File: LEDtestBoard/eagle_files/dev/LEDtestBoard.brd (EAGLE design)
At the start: 30 x 50 mm, 18 parts, among them SW1 PCM12SMTR, SW2 PCM12SMTR, SW3 PCM12SMTR, SW4 PCM12SMTR, SW5 PCM12SMTR, SW6 PCM12SMTR, SW7 PCM12SMTR, SW8 PCM12SMTR

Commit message: Updated LEDtestBoard dev files. Ready to begin pad check and routing.
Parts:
- added D1, D2: SZA05A0A, freddyLibr:SZA05A0A
- added D3: XLAMP_COLOR, freddyLibr:8-SMD-LED
- added D4, D5: LACN5MFBGB241Z, freddyLibr:2-SMD-LED-NO-EXP
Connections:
- net N$6 renamed GND
- new net N$13: D3.1, SW5.2
- new net N$14: D3.2, SW6.2
- new net N$15: D3.3, SW7.2
- new net N$16: D3.4, SW8.2
- new net N$17: D3.8, R5.2
- new net N$18: D3.7, R6.2
- new net N$19: D3.6, R7.2
- new net N$20: D3.5, R8.2
- net N$10: now also D5.2, R4.2; no longer R8.2, SW8.2
- net N$2: now also D1.12, D1.2; no longer SW1.2
- net N$3: now also D1.1, D1.11, SW1.2; no longer R2.2, SW2.2
- net N$4: now also D2.1, D2.11, SW2.2; no longer R3.2, SW3.2
- net N$5: now also D2.12, D2.2, R2.2; no longer R4.2, SW4.2
- net N$7: now also D4.2, R3.2; no longer R5.2, SW5.2
- net N$8: now also D4.1, SW3.2; no longer R6.2, SW6.2
- net N$9: now also D5.1, SW4.2; no longer R7.2, SW7.2
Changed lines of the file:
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@@
 <element name="R7" library="resistor" package="R0603" value="" x="18.86" y="40.48" rot="MR0"/>
 <element name="R8" library="resistor" package="R0603" value="" x="21.23" y="23.14" rot="MR180"/>
+<element name="D3" library="freddyLibr" package="8-SMD-LED" value="XLAMP_COLOR" x="14.64" y="27.42" rot="MR0"/>
+<element name="D4" library="freddyLibr" package="2-SMD-LED-NO-EXP" value="LACN5MFBGB241Z" x="20.6" y="28.05" rot="R270"/>
+<element name="D5" library="freddyLibr" package="2-SMD-LED-NO-EXP" value="LACN5MFBGB241Z" x="19.66" y="21.11" rot="R270"/>
+<element name="D1" library="freddyLibr" package="SZA05A0A" value="SZA05A0A" x="10.5" y="21.13"/>
+<element name="D2" library="freddyLibr" package="SZA05A0A" value="SZA05A0A" x="9.44" y="28.84"/>
 </elements>
 <signals>
@@
 <wire x1="4.18" y1="35.74" x2="4.08" y2="17.38" width="0" layer="19" extent="1-1"/>
 </signal>
-<signal name="N$6">
+<signal name="GND">
 <contactref element="JP1" pad="1"/>
 <contactref element="R1" pad="1"/>
@@
 <contactref element="SW7" pad="3"/>
 <contactref element="SW8" pad="3"/>
-<wire x1="20.12" y1="33.38" x2="25.62" y2="35.62" width="0" layer="19" extent="1-1"/>
-<wire x1="8.2" y1="33.49" x2="20.12" y2="33.38" width="0" layer="19" extent="1-1"/>
-<wire x1="4.18" y1="31.24" x2="8.2" y2="33.49" width="0" layer="19" extent="1-1"/>
-<wire x1="25.5" y1="17.4" x2="20.12" y2="33.38" width="0" layer="19" extent="1-1"/>
+<wire x1="19.71" y1="40.48" x2="24.9" y2="45.85" width="0" layer="19" extent="16-16"/>
+<wire x1="20.12" y1="33.38" x2="19.71" y2="40.48" width="0" layer="19" extent="1-16"/>
+<wire x1="25.62" y1="35.62" x2="20.12" y2="33.38" width="0" layer="19" extent="1-1"/>
+<wire x1="20.38" y1="23.14" x2="20.12" y2="33.38" width="0" layer="19" extent="1-16"/>
+<wire x1="25.63" y1="21.98" x2="20.38" y2="23.14" width="0" layer="19" extent="16-16"/>
+<wire x1="25.5" y1="17.4" x2="25.63" y2="21.98" width="0" layer="19" extent="1-16"/>
 <wire x1="18.54" y1="14.51" x2="25.5" y2="17.4" width="0" layer="19" extent="1-1"/>
 <wire x1="8.72" y1="14.56" x2="18.54" y2="14.51" width="0" layer="19" extent="1-1"/>
 <wire x1="4.08" y1="12.88" x2="8.72" y2="14.56" width="0" layer="19" extent="1-1"/>
 <wire x1="10.5" y1="8" x2="8.72" y2="14.56" width="0" layer="19" extent="1-1"/>
-<wire x1="4.11" y1="26.89" x2="4.08" y2="12.88" width="0" layer="19" extent="1-1"/>
-<wire x1="9.58" y1="45.94" x2="4.11" y2="26.89" width="0" layer="19" extent="1-1"/>
-<wire x1="24.9" y1="45.85" x2="9.58" y2="45.94" width="0" layer="19" extent="1-1"/>
-<wire x1="25.63" y1="21.98" x2="24.9" y2="45.85" width="0" layer="19" extent="1-1"/>
-<wire x1="7.95" y1="23.07" x2="25.63" y2="21.98" width="0" layer="19" extent="1-1"/>
-<wire x1="8.4" y1="40.21" x2="7.95" y2="23.07" width="0" layer="19" extent="1-1"/>
-<wire x1="19.71" y1="40.48" x2="8.4" y2="40.21" width="0" layer="19" extent="1-1"/>
-<wire x1="20.38" y1="23.14" x2="19.71" y2="40.48" width="0" layer="19" extent="1-1"/>
+<wire x1="7.95" y1="23.07" x2="8.72" y2="14.56" width="0" layer="19" extent="1-16"/>
+<wire x1="4.11" y1="26.89" x2="7.95" y2="23.07" width="0" layer="19" extent="16-16"/>
+<wire x1="4.18" y1="31.24" x2="4.11" y2="26.89" width="0" layer="19" extent="1-16"/>
+<wire x1="8.2" y1="33.49" x2="4.18" y2="31.24" width="0" layer="19" extent="1-1"/>
+<wire x1="8.4" y1="40.21" x2="8.2" y2="33.49" width="0" layer="19" extent="1-16"/>
+<wire x1="9.58" y1="45.94" x2="8.4" y2="40.21" width="0" layer="19" extent="16-16"/>
+</signal>
+<signal name="N$13">
+<contactref element="SW5" pad="2"/>
+<contactref element="D3" pad="1"/>
+<wire x1="12.49" y1="29.36" x2="4.11" y2="25.39" width="0" layer="19" extent="1-16"/>
+</signal>
+<signal name="N$14">
+<contactref element="SW6" pad="2"/>
+<contactref element="D3" pad="2"/>
+<wire x1="12.49" y1="28.05" x2="8.08" y2="45.94" width="0" layer="19" extent="1-16"/>
+</signal>
+<signal name="N$15">
+<contactref element="SW7" pad="2"/>
+<contactref element="D3" pad="3"/>
+<wire x1="12.49" y1="26.79" x2="23.4" y2="45.85" width="0" layer="19" extent="1-16"/>
+</signal>
+<signal name="N$16">
+<contactref element="SW8" pad="2"/>
+<contactref element="D3" pad="4"/>
+<wire x1="12.49" y1="25.48" x2="25.63" y2="23.48" width="0" layer="19" extent="1-16"/>
+</signal>
+<signal name="N$17">
+<contactref element="D3" pad="8"/>
+<contactref element="R5" pad="2"/>
+<wire x1="16.79" y1="29.36" x2="7.95" y2="24.77" width="0" layer="19" extent="1-16"/>
+</signal>
+<signal name="N$18">
+<contactref element="D3" pad="7"/>
+<contactref element="R6" pad="2"/>
+<wire x1="16.79" y1="28.05" x2="6.7" y2="40.21" width="0" layer="19" extent="1-16"/>
+</signal>
+<signal name="N$19">
+<contactref element="D3" pad="6"/>
+<contactref element="R7" pad="2"/>
+<wire x1="16.79" y1="26.79" x2="18.01" y2="40.48" width="0" layer="19" extent="1-16"/>
+</signal>
+<signal name="N$20">
+<contactref element="D3" pad="5"/>
+<contactref element="R8" pad="2"/>
+<wire x1="16.79" y1="25.48" x2="22.08" y2="23.14" width="0" layer="19" extent="1-16"/>
 </signal>
 <signal name="N$2">
 <contactref element="R1" pad="2"/>
-<contactref element="SW1" pad="2"/>
-<wire x1="4.08" y1="14.38" x2="10.42" y2="14.56" width="0" layer="19" extent="1-1"/>
+<contactref element="D1" pad="2"/>
+<contactref element="D1" pad="12"/>
+<wire x1="12.35" y1="21.13" x2="10.42" y2="14.56" width="0" layer="19" extent="1-1"/>
+<wire x1="11.9" y1="21.13" x2="12.35" y2="21.13" width="0" layer="19" extent="1-1"/>
 </signal>
 <signal name="N$3">
-<contactref element="R2" pad="2"/>
-<contactref element="SW2" pad="2"/>
-<wire x1="4.18" y1="32.74" x2="9.9" y2="33.49" width="0" layer="19" extent="1-1"/>
+<contactref element="D1" pad="11"/>
+<contactref element="D1" pad="1"/>
+<contactref element="SW1" pad="2"/>
+<wire x1="9.1" y1="21.13" x2="8.65" y2="21.13" width="0" layer="19" extent="1-1"/>
+<wire x1="4.08" y1="14.38" x2="9.1" y2="21.13" width="0" layer="19" extent="1-1"/>
 </signal>
 <signal name="N$4">
-<contactref element="R3" pad="2"/>
-<contactref element="SW3" pad="2"/>
-<wire x1="25.62" y1="34.12" x2="21.82" y2="33.38" width="0" layer="19" extent="1-1"/>
+<contactref element="SW2" pad="2"/>
+<contactref element="D2" pad="11"/>
+<contactref element="D2" pad="1"/>
+<wire x1="8.04" y1="28.84" x2="4.18" y2="32.74" width="0" layer="19" extent="1-1"/>
+<wire x1="7.59" y1="28.84" x2="8.04" y2="28.84" width="0" layer="19" extent="1-1"/>
 </signal>
 <signal name="N$5">
-<contactref element="R4" pad="2"/>
-<contactref element="SW4" pad="2"/>
-<wire x1="25.5" y1="15.9" x2="20.24" y2="14.51" width="0" layer="19" extent="1-1"/>
+<contactref element="D2" pad="2"/>
+<contactref element="D2" pad="12"/>
+<contactref element="R2" pad="2"/>
+<wire x1="11.29" y1="28.84" x2="9.9" y2="33.49" width="0" layer="19" extent="1-1"/>
+<wire x1="10.84" y1="28.84" x2="11.29" y2="28.84" width="0" layer="19" extent="1-1"/>
 </signal>
 <signal name="N$7">
-<contactref element="SW5" pad="2"/>
-<contactref element="R5" pad="2"/>
-<wire x1="4.11" y1="25.39" x2="7.95" y2="24.77" width="0" layer="19" extent="1-1"/>
+<contactref element="R3" pad="2"/>
+<contactref element="D4" pad="2"/>
+<wire x1="19.47" y1="28.05" x2="21.82" y2="33.38" width="0" layer="19" extent="1-1"/>
 </signal>
 <signal name="N$8">
-<contactref element="SW6" pad="2"/>
-<contactref element="R6" pad="2"/>
-<wire x1="8.08" y1="45.94" x2="6.7" y2="40.21" width="0" layer="19" extent="1-1"/>
+<contactref element="D4" pad="1"/>
+<contactref element="SW3" pad="2"/>
+<wire x1="21.73" y1="28.05" x2="25.62" y2="34.12" width="0" layer="19" extent="1-1"/>
 </signal>
 <signal name="N$9">
-<contactref element="SW7" pad="2"/>
-<contactref element="R7" pad="2"/>
-<wire x1="23.4" y1="45.85" x2="18.01" y2="40.48" width="0" layer="19" extent="1-1"/>
+<contactref element="SW4" pad="2"/>
+<contactref element="D5" pad="1"/>
+<wire x1="20.79" y1="21.11" x2="25.5" y2="15.9" width="0" layer="19" extent="1-1"/>
 </signal>
 <signal name="N$10">
-<contactref element="SW8" pad="2"/>
-<contactref element="R8" pad="2"/>
-<wire x1="25.63" y1="23.48" x2="22.08" y2="23.14" width="0" layer="19" extent="1-1"/>
+<contactref element="D5" pad="2"/>
+<contactref element="R4" pad="2"/>
+<wire x1="18.53" y1="21.11" x2="20.24" y2="14.51" width="0" layer="19" extent="1-1"/>
 </signal>
 </signals>

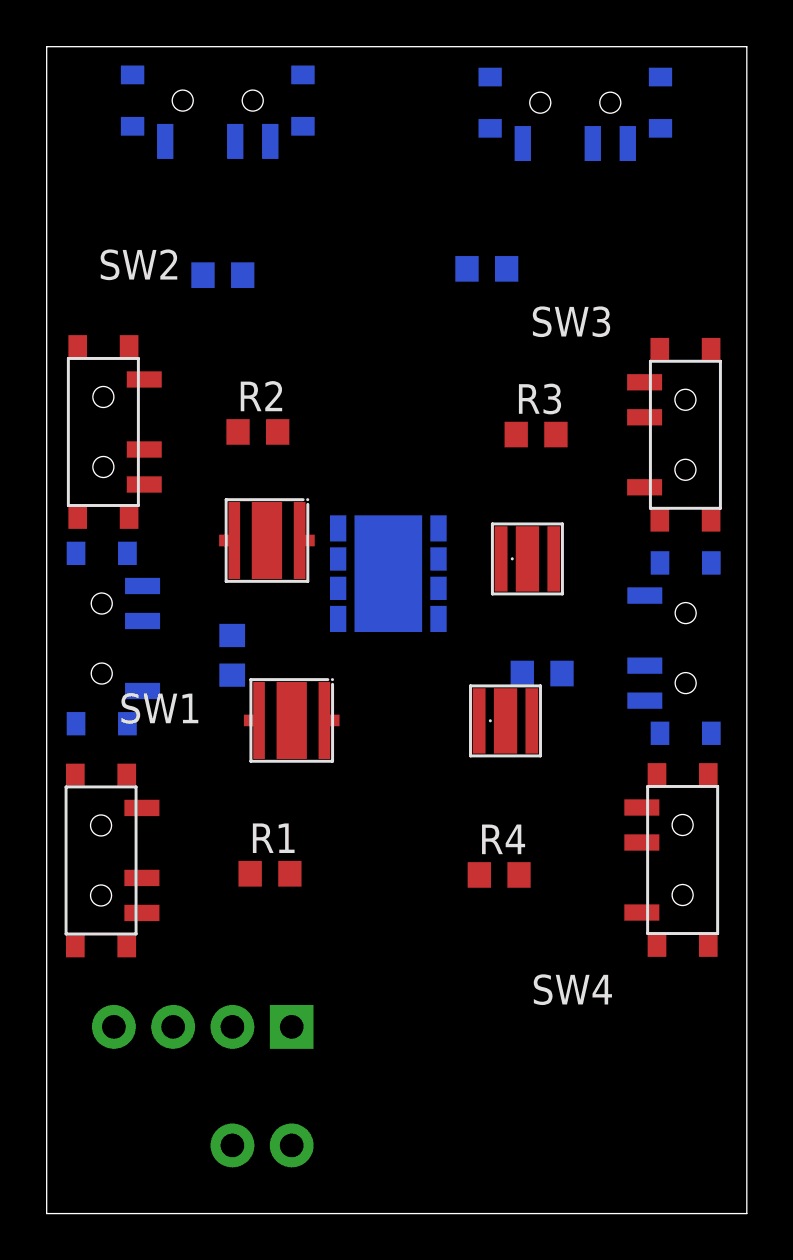
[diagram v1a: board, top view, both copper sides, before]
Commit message: Placed components in approximately precise locations. Ready to begin routing.
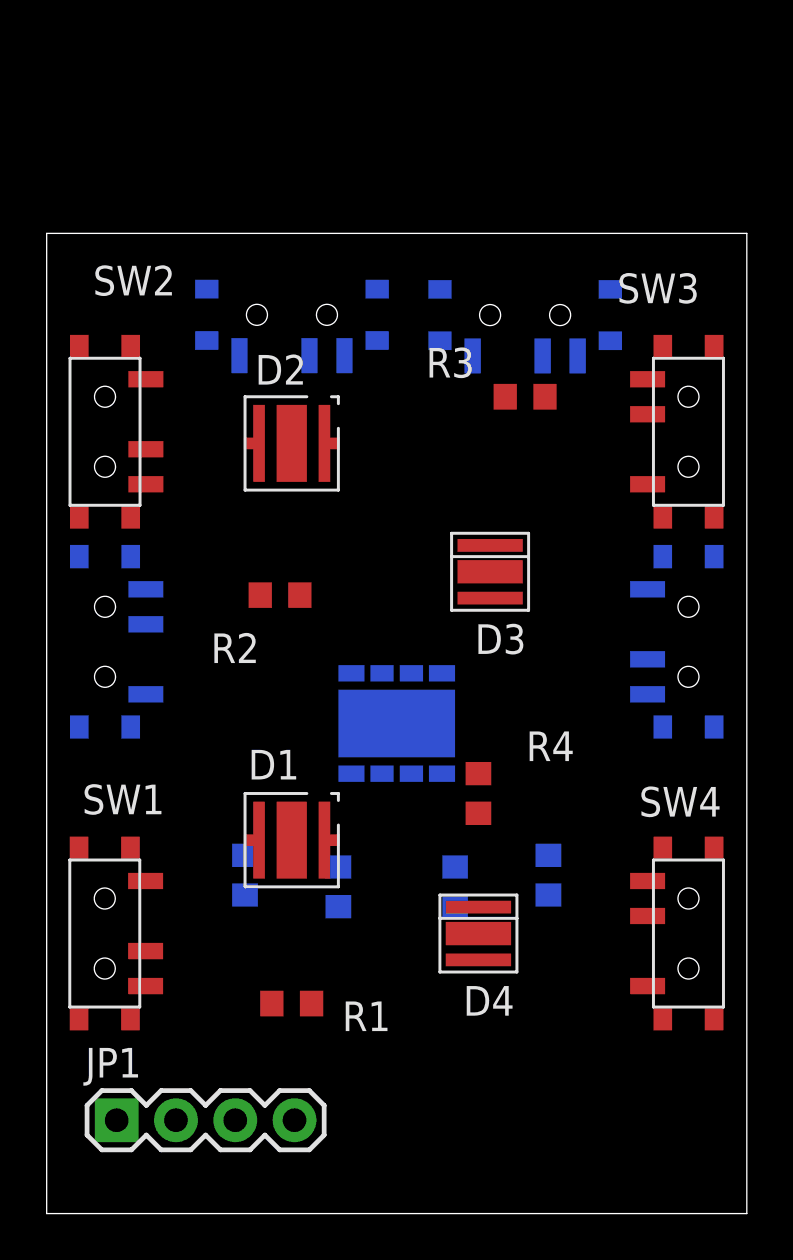
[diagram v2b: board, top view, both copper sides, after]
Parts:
- removed JP2: M02PTH, SparkFun-Connectors:1X02
- D3: value XLAMP_COLOR -> LACN5MFBGB241Z; device freddyLibr:8-SMD-LED -> freddyLibr:2-SMD-LED-NO-EXP
- D5: value LACN5MFBGB241Z -> XLAMP_COLOR; device freddyLibr:2-SMD-LED-NO-EXP -> freddyLibr:8-SMD-LED
- moved R6 28.0 mm to (17.5, 14.0), turned to 270 degrees
- moved R7 27.2 mm to (12.5, 14.0), turned to 90 degrees
- moved SW5 25.1 mm to (27.5, 24.5), turned to 270 degrees
- moved SW8 24.9 mm to (2.50, 24.5), turned to 90 degrees
- moved R5 16.5 mm to (21.5, 14.5)
- moved D4 16.2 mm to (18.5, 12.0), turned to 180 degrees
- moved SW6 16.1 mm to (20.5, 38.5)
- moved R8 15.4 mm to (8.50, 14.5), turned to 90 degrees
- moved SW7 15.2 mm to (10.5, 38.5)
- moved JP1 8.50 mm to (3.00, 4.00), flipped to the top
- moved R2 7.05 mm to (10.0, 26.5)
- moved R1 5.64 mm to (10.5, 9.00)
- moved D1 5.13 mm to (10.5, 16.0)
- moved D5 4.66 mm to (15.0, 21.0), flipped to the bottom, turned to 90 degrees
- moved D3 4.36 mm to (19.0, 27.5), flipped to the top, turned to 180 degrees
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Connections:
- net N$10: now also D4.2; no longer D5.2
- net N$13: now also D5.1; no longer D3.1
- net N$14: now also D5.2; no longer D3.2
- net N$15: now also D5.3; no longer D3.3
- net N$16: now also D5.4; no longer D3.4
- net N$17: now also D5.8; no longer D3.8
- net N$18: now also D5.7; no longer D3.7
- net N$19: now also D5.6; no longer D3.6
- net N$20: now also D5.5; no longer D3.5
- net N$7: now also D3.2; no longer D4.2
- net N$8: now also D3.1; no longer D4.1
- net N$9: now also D4.1; no longer D5.1
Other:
- board size 30 x 50 mm -> 30 x 42 mm

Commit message: All routed.
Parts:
- moved SW1 0.11 mm to (2.60, 12.0)
- moved SW3 0.10 mm to (27.4, 33.5)
- moved SW4 0.10 mm to (27.4, 12.0)
- moved SW5 0.10 mm to (27.4, 24.5)
- moved SW2 0.10 mm to (2.60, 33.5)
- moved SW8 0.10 mm to (2.60, 24.5)
- turned R6 to 90 degrees
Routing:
- net GND: track 0.00 -> 122.2 mm, vias 0 -> 5
- net N$1: track 0.00 -> 118.0 mm, vias 0 -> 7
- net N$14: track 0.00 -> 15.9 mm
- net N$15: track 0.00 -> 14.9 mm
- net N$8: track 0.00 -> 13.1 mm
- net N$16: track 0.00 -> 9.58 mm
- net N$13: track 0.00 -> 8.96 mm
- net N$9: track 0.00 -> 7.96 mm
- net N$2: track 0.00 -> 7.41 mm
- net N$4: track 0.00 -> 7.32 mm
- net N$5: track 0.00 -> 7.12 mm
- net N$3: track 0.00 -> 6.72 mm
- net N$20: track 0.00 -> 6.65 mm
- net N$7: track 0.00 -> 6.64 mm
- net N$17: track 0.00 -> 6.60 mm
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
